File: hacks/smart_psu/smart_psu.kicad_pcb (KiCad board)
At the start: 2 copper layers, 26 parts, among them IC1 ATTINY85-P, P1 USB_OTG, P2 External DC, P3 VCC, P4 Battery, Q1 Q_NMOS_DGS, SW1 Reset, SW2 On/Off, SW3 Voltage, U1 MAX1555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

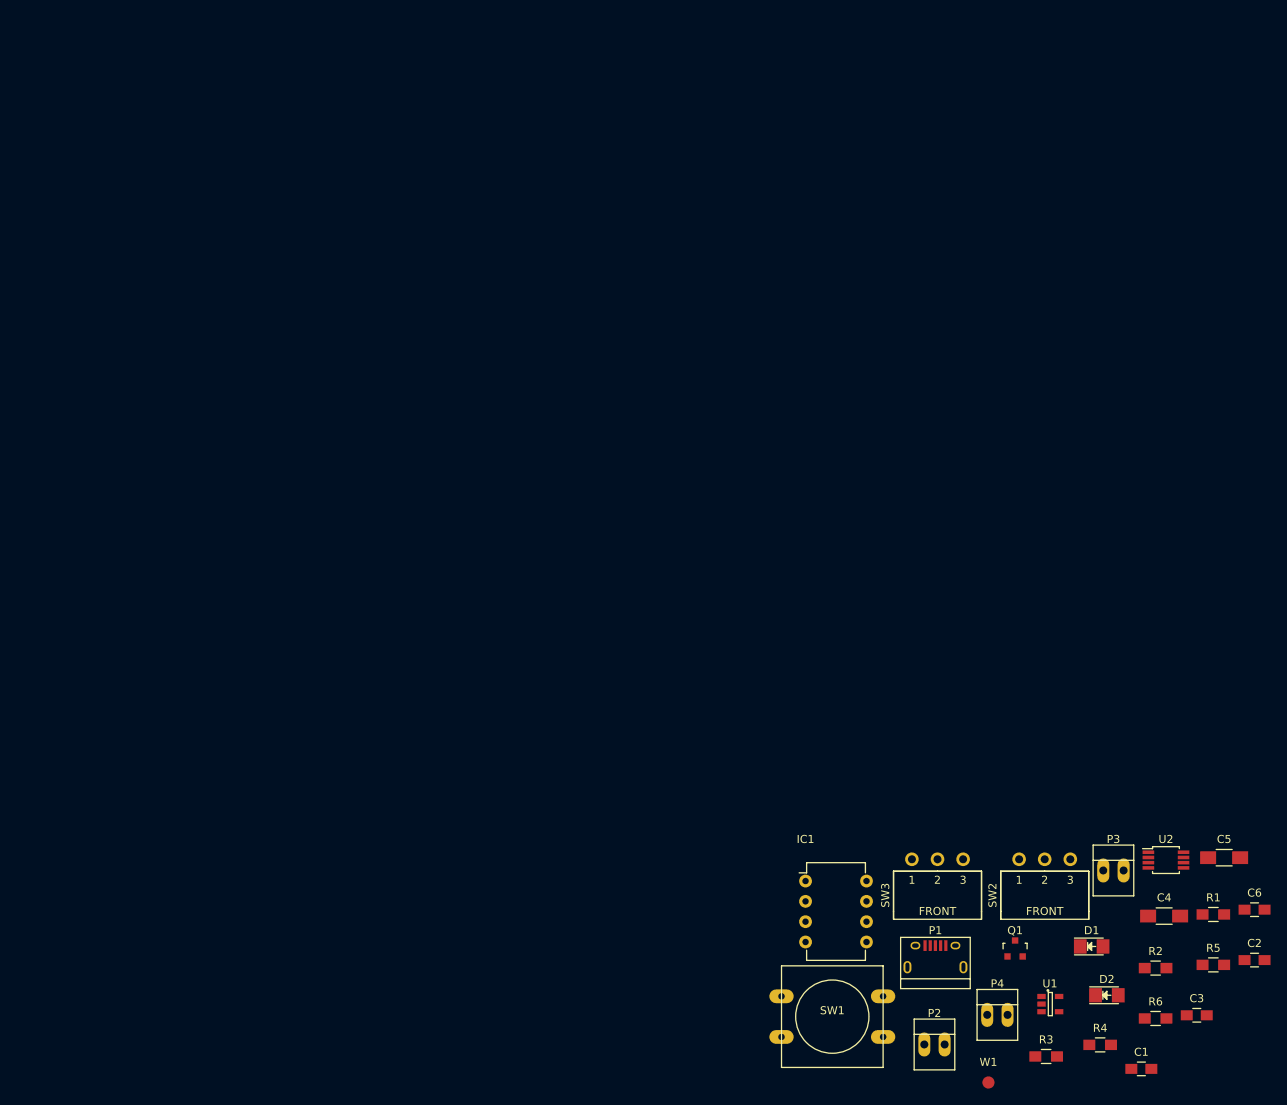
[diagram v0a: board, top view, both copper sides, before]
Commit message: started laying out pcb
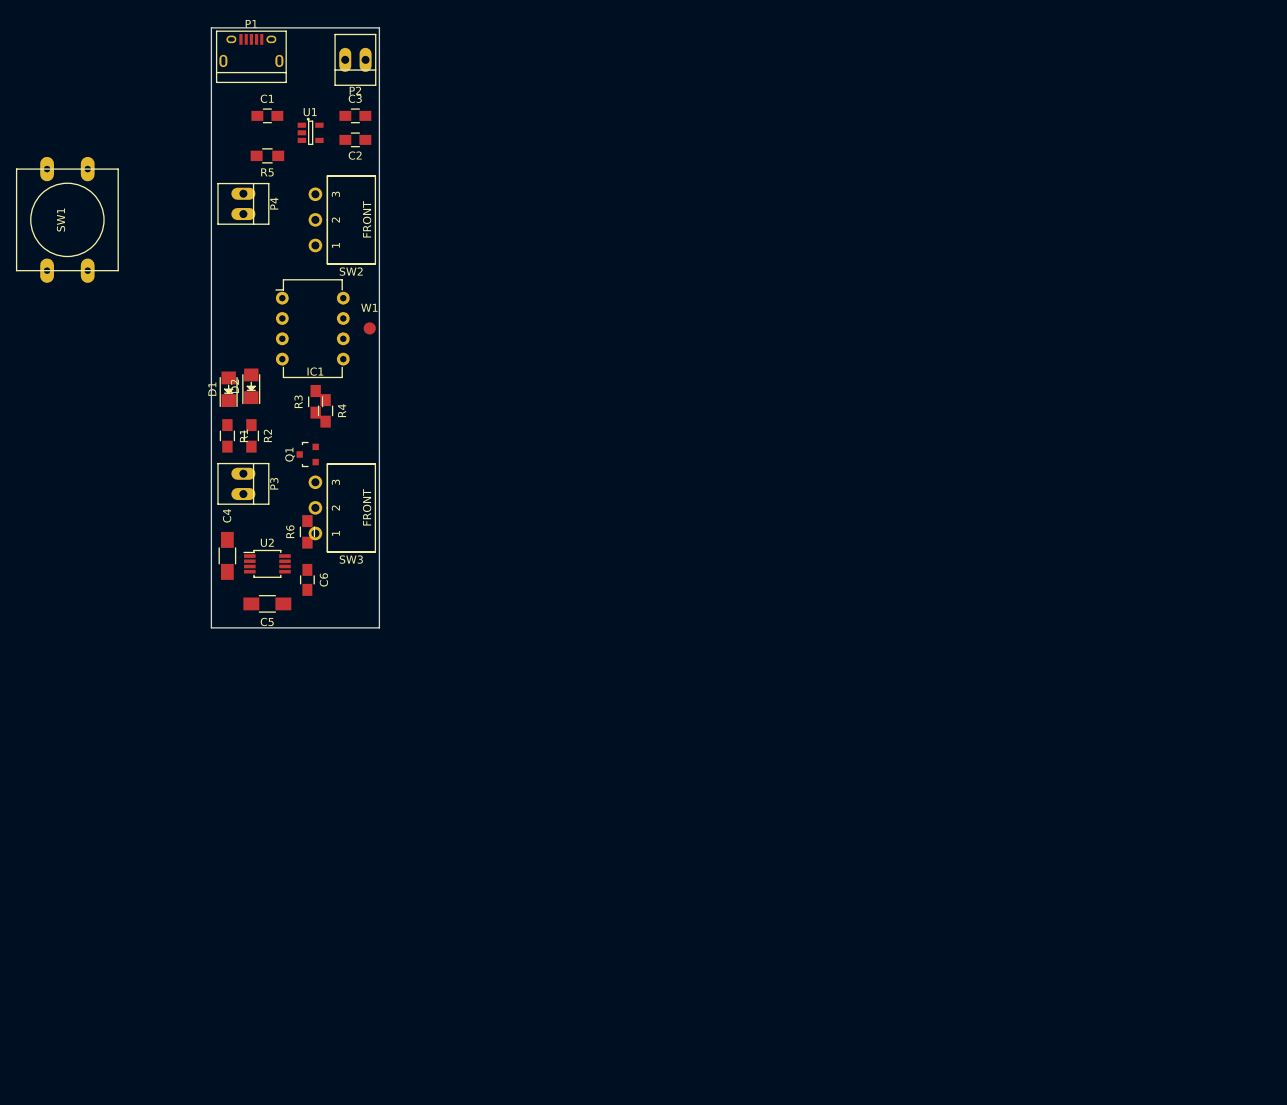
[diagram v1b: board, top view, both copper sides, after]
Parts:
- moved C1 161.6 mm to (67.0, 25.0)
- moved R5 155.6 mm to (67.0, 30.0), turned to 180 degrees
- moved C3 154.0 mm to (78.0, 25.0)
- moved C2 152.1 mm to (78.0, 28.0)
- moved U1 142.9 mm to (72.4, 27.1)
- moved P2 142.8 mm to (78.0, 18.0), turned to 180 degrees
- moved P1 141.9 mm to (65.0, 17.0)
- moved P4 138.4 mm to (64.0, 36.0), turned to 270 degrees
- moved SW1 138.1 mm to (42.0, 38.0), turned to 90 degrees
- moved R1 137.0 mm to (62.0, 65.0), turned to 270 degrees
- moved D2 131.3 mm to (65.0, 58.8), turned to 90 degrees
- moved R2 131.1 mm to (65.0, 65.0), turned to 270 degrees
- moved D1 128.4 mm to (62.2, 59.2), turned to 90 degrees
- moved C4 125.5 mm to (62.0, 80.0), turned to 270 degrees
- moved C6 125.4 mm to (72.0, 83.0), turned to 270 degrees
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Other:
- board outline added: 21 x 75 mm

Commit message: pcb layouayout done
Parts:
- ?: renamed from W1; value TEST_1P -> PB1
- C1, C2, C3, C6: value 1uF -> (none)
- C4, C5: value 10uF -> (none)
- D1: value GREEN_LED -> (none)
- D2: value RED_LED -> (none)
- P1: value USB_OTG -> USB
- P3: value VCC -> Output; footprint Connect:PINHEAD1-2 -> Connect:PINHEAD1-3
- Q1: value Q_NMOS_DGS -> NMOS
- R1, R2: value 3.3K -> (none)
- R3, R4: value 1K -> (none)
- R5, R6: value 100K -> (none)
- SW1: footprint Buttons_Switches_ThroughHole:SW_PUSH-12mm -> Buttons_Switches_SMD:SW_SPST_PTS645
- moved SW1 22.3 mm to (63.8, 42.6)
- moved R4 5.39 mm to (69.6, 59.1), turned to 90 degrees
- moved D1 4.62 mm to (62.0, 54.5)
- moved R2 4.36 mm to (65.1, 60.6)
- moved R1 4.36 mm to (62.0, 60.6)
- moved D2 4.26 mm to (65.1, 54.5)
- moved Q1 3.65 mm to (70.7, 63.9)
- moved R5 3.61 mm to (65.0, 27.0)
- moved R6 3.35 mm to (73.5, 80.0), turned to 0 degrees
- moved SW2 3.00 mm to (73.0, 35.0)
- moved SW3 3.00 mm to (73.0, 71.0)
- moved IC1 2.94 mm to (69.4, 44.9)
- moved P4 2.29 mm to (63.8, 33.7), turned to 90 degrees
- moved C2 2.24 mm to (76.0, 27.0)
- moved C3 2.11 mm to (76.0, 24.3)
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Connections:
- P1 pad 2: Net-(P1-Pad2) -> (no net)
- P1 pad 3: Net-(P1-Pad3) -> (no net)
- P1 pad 4: Net-(P1-Pad4) -> (no net)
- P3 pad 1: VCC -> +BATT
- P3 pad 2: GNDA -> VCC
- SW2 pad 1: Net-(SW2-Pad1) -> (no net)
- U2 pad 1: Net-(U2-Pad1) -> (no net)
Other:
- board text added: "+BATT"
- board text added: "GNDA"
- board text added: "VCC"

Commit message: started laying tracks
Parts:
- moved C3 3.06 mm to (75.7, 27.4)
- moved C2 2.19 mm to (75.7, 24.8)
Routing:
- net Net-(C1-Pad2): track 0.00 -> 8.15 mm
- net Net-(IC1-Pad7): track 0.00 -> 3.19 mm
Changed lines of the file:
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@@
   (general
     (links 53)
-    (no_connects 53)
+    (no_connects 50)
     (area 59.924999 13.924999 81.075001 89.075001)
     (thickness 1.6)
     (drawings 7)
-    (tracks 0)
+    (tracks 9)
     (zones 0)
     (modules 26)
@@
   )
   (module Capacitors_SMD:C_0805_HandSoldering (layer F.Cu)
-    (at 76 27)
+    (at 75.744 24.828)
     (descr "Capacitor SMD 0805, hand soldering")
     (tags "capacitor 0805")
@@
   )
   (module Capacitors_SMD:C_0805_HandSoldering (layer F.Cu)
-    (at 75.998 24.32)
+    (at 75.744 27.368)
     (descr "Capacitor SMD 0805, hand soldering")
     (tags "capacitor 0805")
@@
   (gr_line (start 60 89) (end 81 89) (angle 90) (layer Edge.Cuts) (width 0.15))
   (gr_line (start 60 14) (end 60 89) (angle 90) (layer Edge.Cuts) (width 0.15))
+  (segment (start 66.1229 19.78654) (end 66.1229 24.1169) (width 0.25) (layer F.Cu) (net 2))
+  (segment (start 66.1229 24.1169) (end 66.326 24.32) (width 0.25) (layer F.Cu) (net 2))
+  (segment (start 66.326 24.32) (end 67.616 24.32) (width 0.25) (layer F.Cu) (net 2))
+  (segment (start 67.616 24.32) (end 68.961 25.665) (width 0.25) (layer F.Cu) (net 2))
+  (segment (start 68.961 25.665) (end 69.305952 25.665) (width 0.25) (layer F.Cu) (net 2))
+  (segment (start 74.24 24.574) (end 74.494 24.828) (width 0.25) (layer F.Cu) (net 3))
+  (segment (start 66.35 27) (end 67.502 27) (width 0.25) (layer F.Cu) (net 15))
+  (segment (start 68.067 27.565) (end 69.305952 27.565) (width 0.25) (layer F.Cu) (net 15))
+  (segment (start 67.502 27) (end 68.067 27.565) (width 0.25) (layer F.Cu) (net 15))
 )

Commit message: first iteration ready
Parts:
- moved ? 6.84 mm to (77.3, 56.3)
- moved P1 2.79 mm to (67.6, 18.2)
- moved P2 0.23 mm to (77.8, 17.5)
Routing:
- net GND: track 0.00 -> 130.0 mm, vias 0 -> 4
- net +BATT: track 0.00 -> 118.6 mm, vias 0 -> 2
- net GNDA: track 0.00 -> 45.5 mm, vias 0 -> 1
- net Net-(IC1-Pad7): track 3.19 -> 32.8 mm
- net Net-(C2-Pad1): track 0.36 -> 20.0 mm
- net VCC: track 0.00 -> 15.7 mm
- net Net-(SW3-Pad2): track 0.00 -> 12.2 mm
- net Net-(IC1-Pad1): track 0.00 -> 12.0 mm
- net Net-(P1-Pad6): track 0.00 -> 11.2 mm
- net Net-(D1-Pad2): track 0.00 -> 10.5 mm
- net Net-(P4-Pad1): track 0.00 -> 10.5 mm
- net Net-(IC1-Pad6): track 0.00 -> 7.59 mm
- net Net-(IC1-Pad5): track 0.00 -> 7.25 mm
- net Net-(D2-Pad2): track 0.00 -> 6.67 mm
- net Net-(Q1-Pad2): track 0.00 -> 5.28 mm
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- added copper zone on B.Cu, net GND
- added copper zone on B.Cu, net GNDA
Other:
- board text added: "Smart PSU v0.1 by @mik4el4ndersson 2016 Selectable 5v or 3.3v output USB and external charging of 1S Li-ion battery Attiny85 enabling smart control Output max 100mA VCC and max 1000mA +BATT"

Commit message: printed out layout to verify
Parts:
- IC1: value ATTINY85-P -> (none)
- P2: value External DC -> Ext DC
- Q1: value NMOS -> (none)
- U1: value MAX1555 -> (none)
- U2: value MCP1253 -> (none)
- moved Q1 0.92 mm to (69.9, 64.5), turned to 180 degrees
- moved P2 0.68 mm to (77.6, 16.8), turned to 270 degrees
- turned P4 to 270 degrees
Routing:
- net GND: track 130.0 -> 77.6 mm, vias 4 -> 3
- net Net-(C2-Pad1): track 20.0 -> 12.5 mm
- net Net-(Q1-Pad2): track 5.28 -> 6.76 mm
- net GNDA: track 45.5 -> 46.2 mm
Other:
- board text added: "+"
- board text added: "-"
- board text added: "3.3V"
- board text added: "5V"
- board text added: "GND"
- board text added: "OFF"
- board text added: "ON"

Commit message: fixed exports and ordered pcb v01
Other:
- rule pad_to_mask_clearance: 0.2 -> 0.0762
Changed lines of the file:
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@@
     (pad_size 0.8001 0.8001)
     (pad_drill 0)
-    (pad_to_mask_clearance 0.2)
+    (pad_to_mask_clearance 0.0762)
     (aux_axis_origin 0 0)
     (grid_origin 92 131)
     (visible_elements FFFFFF7F)
     (pcbplotparams
-      (layerselection 0x3fffc_80000001)
+      (layerselection 0x010f0_80000001)
       (usegerberextensions true)
       (excludeedgelayer true)
@@
       (plotinvisibletext false)
       (padsonsilk false)
-      (subtractmaskfromsilk false)
+      (subtractmaskfromsilk true)
       (outputformat 1)
       (mirror false)
@@
     (descr "C&K Components SPST SMD PTS645 Series 6mm Tact Switch")
     (tags "SPST Button Switch")
-    (fp_text reference SW1 (at 0 -0.8 90) (layer F.SilkS)
-      (effects (font (size 1 1) (thickness 0.15)))
-    )
+    (fp_text reference SW1 (at 0.008 -0.106 90) (layer F.SilkS)
+      (effects (font (size 1 1) (thickness 0.15)))
+    )
